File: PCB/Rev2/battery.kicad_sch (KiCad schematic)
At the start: 11 parts, among them U2 TP4057, U3 TPS2116DRL, U4 TPS2116DRL

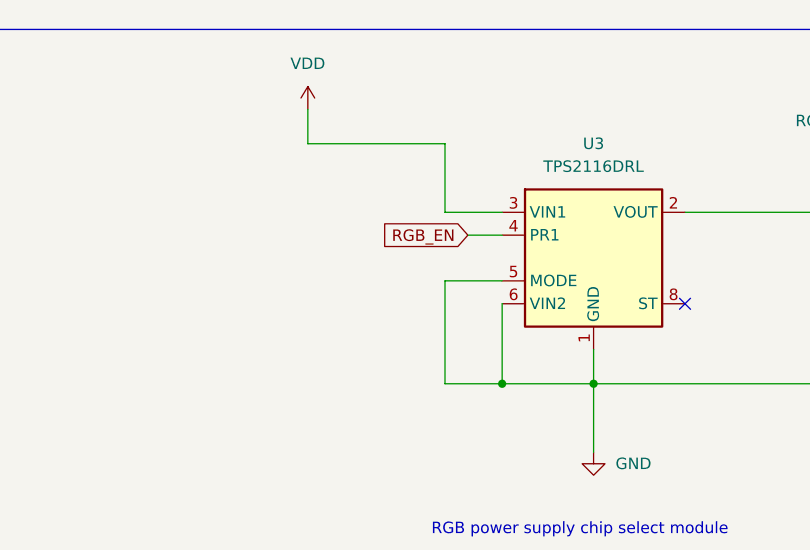
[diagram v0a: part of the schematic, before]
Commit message: Change tps2116 mode
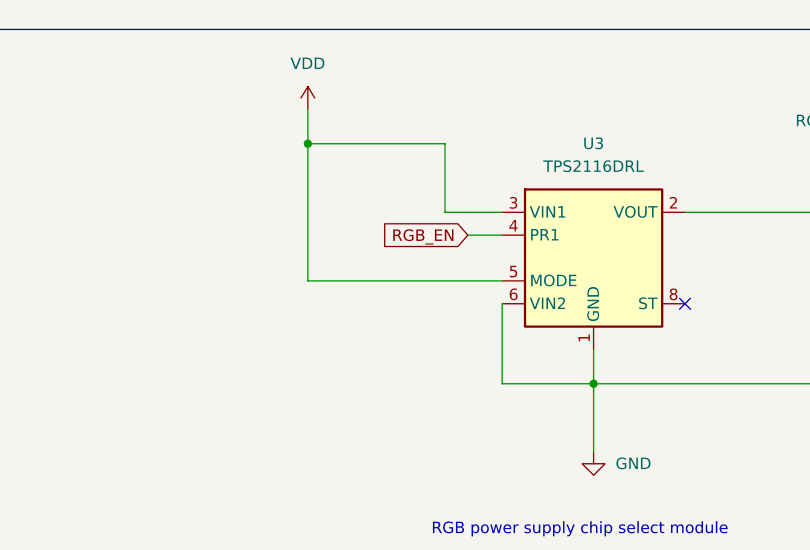
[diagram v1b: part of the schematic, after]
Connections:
- net GND: no longer U3.5 (MODE)
- net VDD: now also U3.5 (MODE)
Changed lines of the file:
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@@
 	)
 	(junction
-		(at 161.29 52.07)
+		(at 139.7 25.4)
 		(diameter 0)
 		(color 0 0 0 0)
@@
 	(wire
 		(pts
-			(xy 154.94 52.07) (xy 161.29 52.07)
-		)
-		(stroke
-			(width 0)
-			(type default)
-		)
-	)
-	(wire
-		(pts
 			(xy 171.45 107.95) (xy 198.12 107.95)
 		)
@@
 	(wire
 		(pts
-			(xy 154.94 40.64) (xy 154.94 52.07)
-		)
-		(stroke
-			(width 0)
-			(type default)
-		)
-	)
-	(wire
-		(pts
 			(xy 198.12 86.36) (xy 198.12 91.44)
 		)
@@
 	(wire
 		(pts
+			(xy 139.7 25.4) (xy 139.7 40.64)
+		)
+		(stroke
+			(width 0)
+			(type default)
+		)
+	)
+	(wire
+		(pts
 			(xy 161.29 101.6) (xy 161.29 114.3)
 		)
@@
 	(wire
 		(pts
+			(xy 139.7 40.64) (xy 161.29 40.64)
+		)
+		(stroke
+			(width 0)
+			(type default)
+		)
+	)
+	(wire
+		(pts
 			(xy 59.69 52.07) (xy 59.69 55.88)
 		)
@@
 		)
 		(stroke
-			(width 0)
-			(type default)
-		)
-	)
-	(wire
-		(pts
-			(xy 154.94 40.64) (xy 161.29 40.64)
-		)
-		(stroke
